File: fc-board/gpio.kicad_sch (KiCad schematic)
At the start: 28 parts, among them J14 Micro_SD_Card_Det2, U1 KS4GRI-806C-32, U2 RT9742GGJ5, U3 749023310, U4 74LVC1G07SE-7, X1 microSD-card

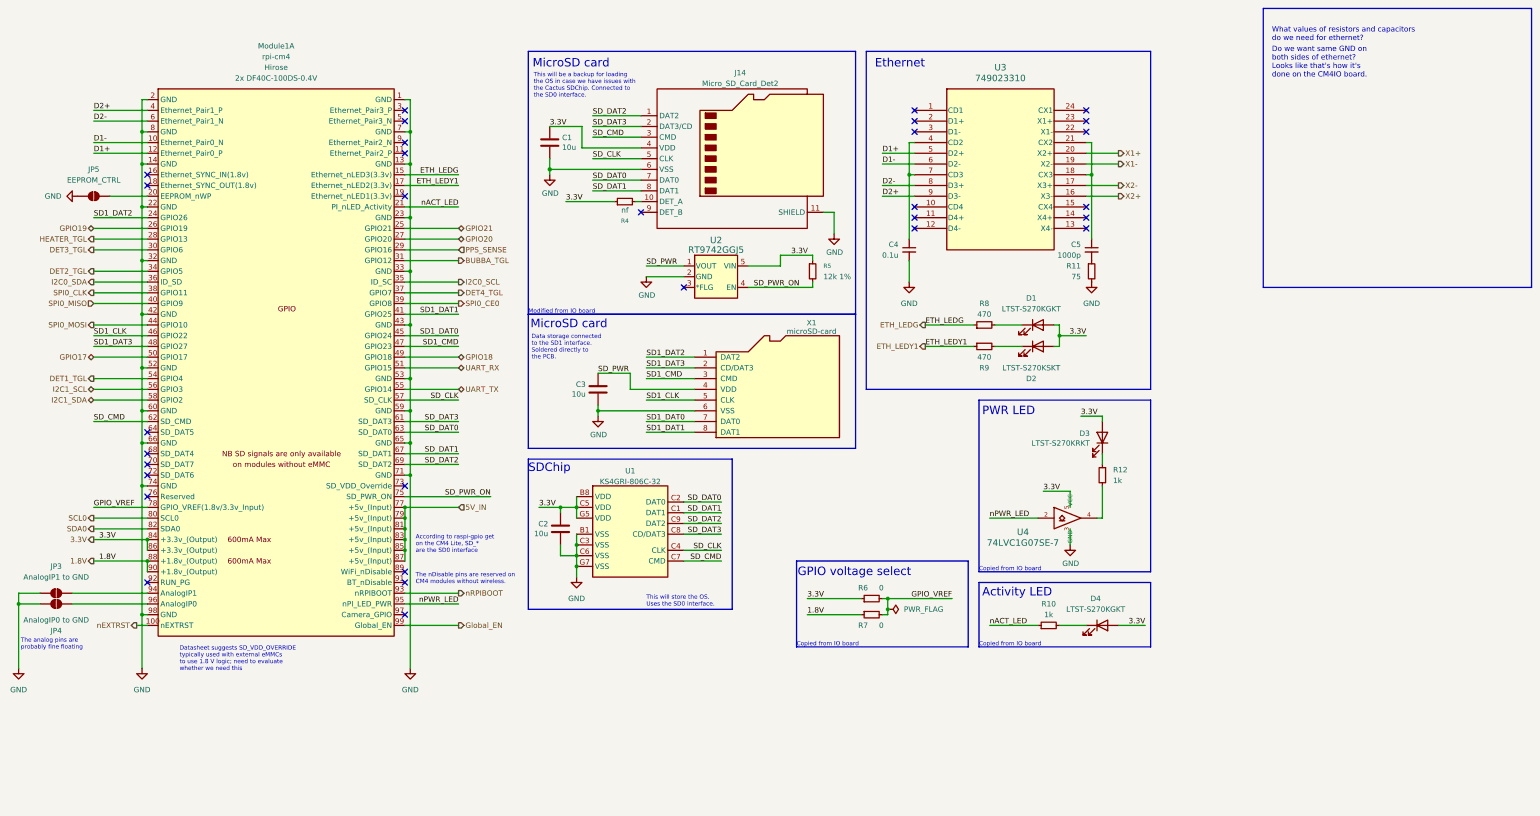
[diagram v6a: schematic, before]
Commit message: Fixed incorrect routes, modified gondola eth, cosmetics
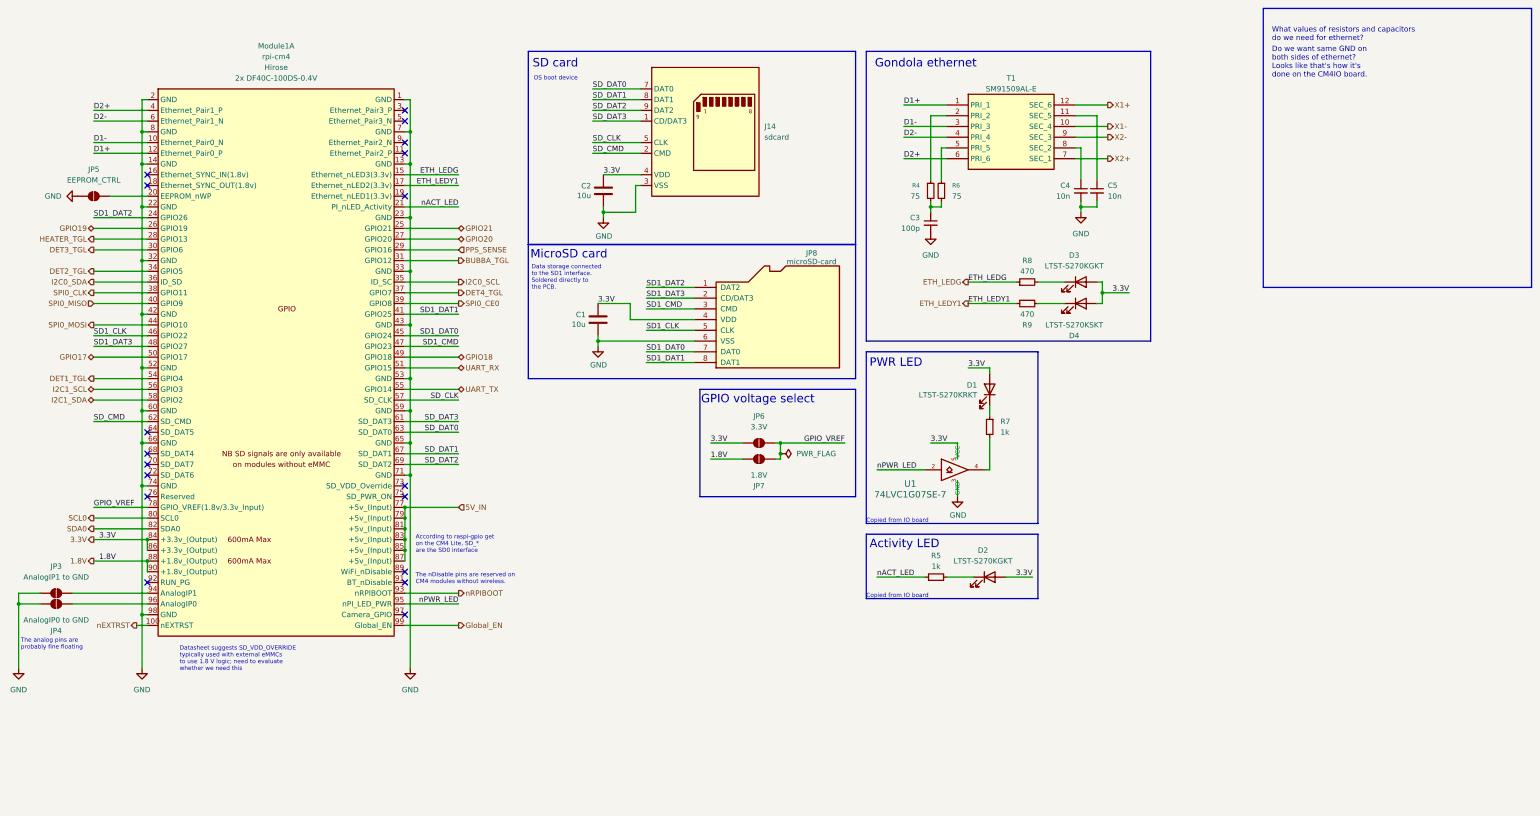
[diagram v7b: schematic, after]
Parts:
- removed C2: 10u, Capacitor_SMD:C_1206_3216Metric, symbol Device:C
- removed J14: Micro_SD_Card_Det2, fc-board:molex-503398-1892, symbol fc-board:Micro_SD_Card_Det2
- removed R11: 75, Resistor_SMD:R_1206_3216Metric, symbol Device:R_Small
- removed R5: 12k 1%, Resistor_SMD:R_1206_3216Metric, symbol Device:R_Small
- removed R7: 0, Resistor_SMD:R_1206_3216Metric_Pad1.30x1.75mm_HandSolder, symbol Device:R_Small
- removed U1: KS4GRI-806C-32, fc-board:KS4GRI-806C-32, symbol fc-board:KS4GRI-806C-32
- removed U2: RT9742GGJ5, fc-board:RT9742GGJ5, symbol fc-board:RT9742GGJ5
- removed U3: 749023310, fc-board:749023310, symbol fc-board:749023310
- added C3: 100p, Capacitor_SMD:C_1206_3216Metric, symbol Device:C_Small
- added J14: sdcard, fc-board:sdcard, symbol fc-board:sdcard
- added JP6: 3.3V, Jumper:SolderJumper-2_P1.3mm_Open_Pad1.0x1.5mm, symbol Jumper:SolderJumper_2_Open
- added JP7: 1.8V, Jumper:SolderJumper-2_P1.3mm_Open_Pad1.0x1.5mm, symbol Jumper:SolderJumper_2_Open
- added T1: SM91509AL-E, fc-board:SM91509AL-E, symbol fc-board:SM91509AL-E
- C4: value 0.1u -> 10n
- C5: value 1000p -> 10n
- R4: value nf -> 75
- R6: value 0 -> 75
- renumbered C3 to C1, C1 to C2, D3 to D1, D4 to D2, D1 to D3, D2 to D4, X1 to JP8, R10 to R5, R12 to R7, U4 to U1
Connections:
- net SD_PWR is gone; now on net 3.3V: C1.1, JP8.4 (VDD)
- net 1.8V: now also JP7.1 (A)
- net 3.3V: now also J14.4 (VDD), JP6.1 (A); no longer R4.1, R6.1
- net D1+: now also T1.1 (PRI_1)
- net D1-: now also T1.3 (PRI_3)
- net D2+: now also T1.6 (PRI_6)
- net D2-: now also T1.4 (PRI_4)
- net GND: now also C5.2, C3.2, J14.3 (VSS), J14.6 (VSS)
- net GPIO_VREF: now also JP6.2 (B), JP7.2 (B); no longer R6.2
- net SD_CLK: now also J14.5 (CLK)
- net SD_CMD: now also J14.2 (CMD)
- net SD_DAT0: now also J14.7 (DAT0)
- net SD_DAT1: now also J14.8 (DAT1)
- net SD_DAT2: now also J14.9 (DAT2)
- net SD_DAT3: now also J14.1 (CD/DAT3)
- net X1+: now also T1.12 (SEC_6)
- net X1-: now also T1.10 (SEC_4)
- net X2+: now also T1.7 (SEC_1)
- net X2-: now also T1.9 (SEC_3)
- net at R4.2: now also R6.2, C3.1
- net at C5.1: now also T1.11 (SEC_5)
- net at C4.1: now also T1.8 (SEC_2)
- net SD_PWR_ON: no longer names the net of Module1.75 (SD_PWR_ON)
- new net: R6.1, T1.5 (PRI_5)
- new net: R4.1, T1.2 (PRI_2)
- no-connect marks 31 -> 18
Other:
- note added: "Gondola ethernet"
- note added: "OS boot device"
- note added: "SD card"
- note removed: "Ethernet"
- note removed: "Modified from IO board"
- note removed: "SDChip"
- note removed: "This will be a backup for loading the OS in case we have issues with the Cactus SDChip. Connected to the SD0 interface."
- note removed: "This will store the OS. Uses the SD0 interface."
- moved on the sheet: C1, C2, D1, D2, D3, D4, JP8, R5, R7, R8, R9, U1

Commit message: Fixed PCIe routing, voltage sensing, added DAQ toggle, LCT interrupt, bias sensing resistors, SD card, and more
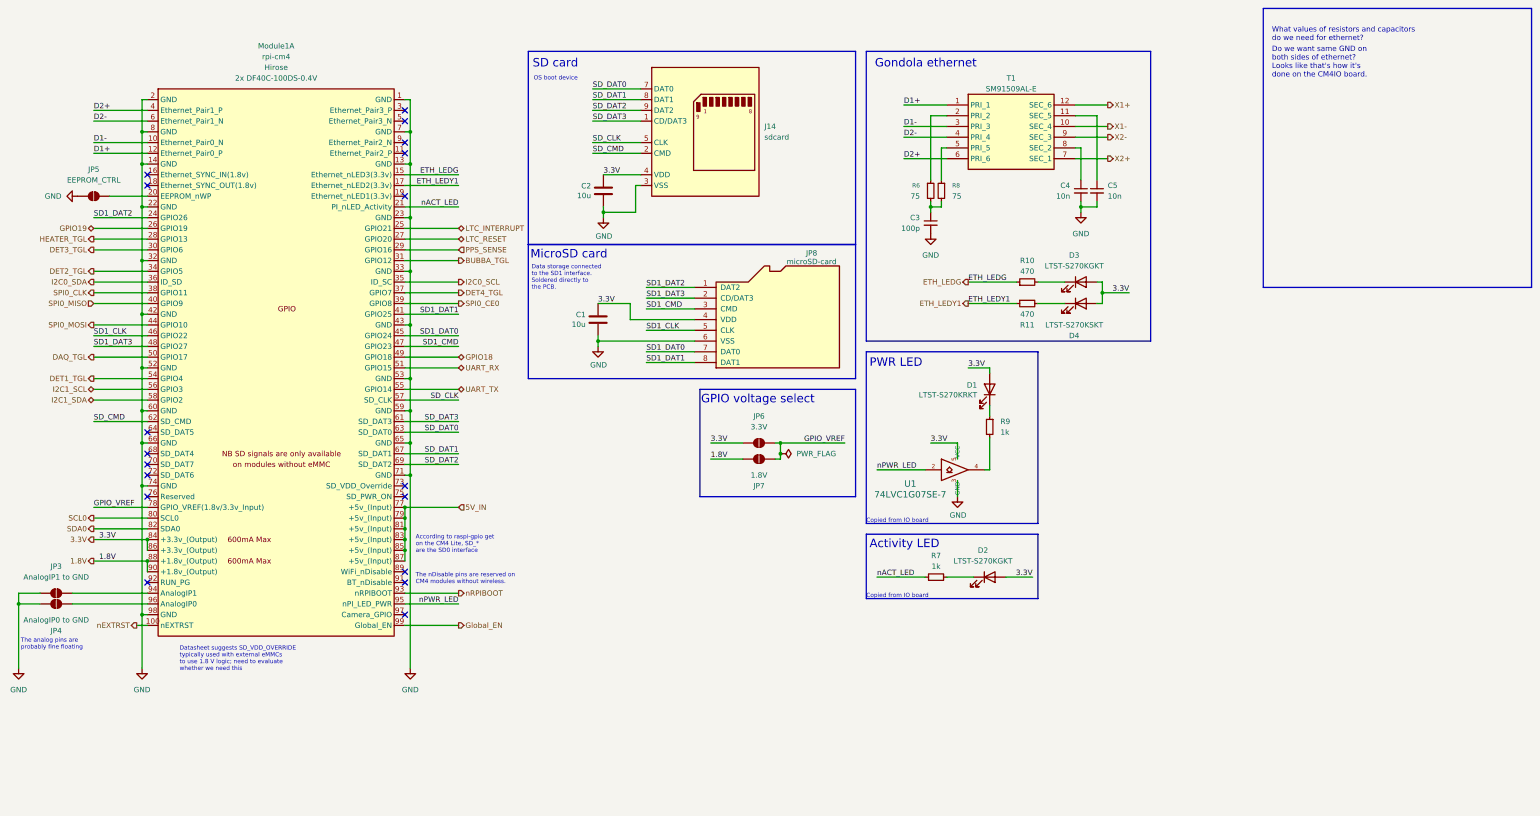
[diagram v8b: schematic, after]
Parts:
- renumbered R8 to R10, R9 to R11, R4 to R6, R5 to R7, R6 to R8, R7 to R9
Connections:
- net GPIO17 renamed DAQ_TGL
- net GPIO20 renamed LTC_RESET
- net GPIO21 renamed LTC_INTERRUPT
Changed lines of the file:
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@@
 		)
 	)
+	(hierarchical_label "LTC_INTERRUPT"
+		(shape bidirectional)
+		(at 118.11 57.15 0)
+		(effects
+			(font
+				(size 1.27 1.27)
+			)
+			(justify left)
+		)
+	)
 	(hierarchical_label "DET3_TGL"
 		(shape output)
@@
 		)
 	)
-	(hierarchical_label "PPS_SENSE"
-		(shape input)
-		(at 118.11 62.23 0)
+	(hierarchical_label "LTC_RESET"
+		(shape bidirectional)
+		(at 118.11 59.69 0)
 		(effects
 			(font
@@
 		)
 	)
-	(hierarchical_label "GPIO20"
-		(shape bidirectional)
-		(at 118.11 59.69 0)
+	(hierarchical_label "PPS_SENSE"
+		(shape input)
+		(at 118.11 62.23 0)
 		(effects
 			(font
@@
 		)
 	)
-	(hierarchical_label "GPIO17"
-		(shape bidirectional)
+	(hierarchical_label "DAQ_TGL"
+		(shape output)
 		(at 31.75 87.63 180)
 		(effects
@@
 		)
 	)
-	(hierarchical_label "GPIO21"
-		(shape bidirectional)
-		(at 118.11 57.15 0)
-		(effects
-			(font
-				(size 1.27 1.27)
-			)
-			(justify left)
-		)
-	)
 	(symbol
 		(lib_id "Device:C")
@@
 		(on_board yes)
 		(dnp no)
-		(property "Reference" "R9"
+		(property "Reference" "R11"
 			(at 252.73 80.01 90)
 			(effects
@@
 			(project "fc-board"
 				(path "/14bbabed-904f-4efc-8ba4-be00e59385c4/21f70e3e-098f-47c8-b8cd-a351aace6ca2"
-					(reference "R9")
+					(reference "R11")
 					(unit 1)
 				)
@@
 		(on_board yes)
 		(dnp no)
-		(property "Reference" "R7"
+		(property "Reference" "R9"
 			(at 246.38 102.8699 0)
 			(effects
@@
 			(project "fc-board"
 				(path "/14bbabed-904f-4efc-8ba4-be00e59385c4/21f70e3e-098f-47c8-b8cd-a351aace6ca2"
-					(reference "R7")
+					(reference "R9")
 					(unit 1)
 				)
@@
 		(on_board yes)
 		(dnp no)
-		(property "Reference" "R6"
+		(property "Reference" "R8"
 			(at 234.95 46.9899 0)
 			(effects
@@
 			(project ""
 				(path "/14bbabed-904f-4efc-8ba4-be00e59385c4/21f70e3e-098f-47c8-b8cd-a351aace6ca2"
-					(reference "R6")
+					(reference "R8")
 					(unit 1)
 				)
@@
 		(on_board yes)
 		(dnp no)
-		(property "Reference" "R4"
+		(property "Reference" "R6"
 			(at 227.33 46.9899 0)
 			(effects
@@
 			(project ""
 				(path "/14bbabed-904f-4efc-8ba4-be00e59385c4/21f70e3e-098f-47c8-b8cd-a351aace6ca2"
-					(reference "R4")
+					(reference "R6")
 					(unit 1)
 				)
@@
 		(dnp no)
 		(fields_autoplaced yes)
-		(property "Reference" "R5"
+		(property "Reference" "R7"
 			(at 231.14 134.62 90)
 			(effects
@@
 			(project "fc-board"
 				(path "/14bbabed-904f-4efc-8ba4-be00e59385c4/21f70e3e-098f-47c8-b8cd-a351aace6ca2"
-					(reference "R5")
+					(reference "R7")
 					(unit 1)
 				)
@@
 		(dnp no)
 		(fields_autoplaced yes)
-		(property "Reference" "R8"
+		(property "Reference" "R10"
 			(at 252.73 64.77 90)
 			(effects
@@
 			(project ""
 				(path "/14bbabed-904f-4efc-8ba4-be00e59385c4/21f70e3e-098f-47c8-b8cd-a351aace6ca2"
-					(reference "R8")
+					(reference "R10")
 					(unit 1)
 				)
